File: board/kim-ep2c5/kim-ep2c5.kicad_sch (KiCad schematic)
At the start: 4 parts, among them J101 Conn_02x20_Odd_Even, J102 Conn_01x16_Male, J103 TTY, U101 EP2C5

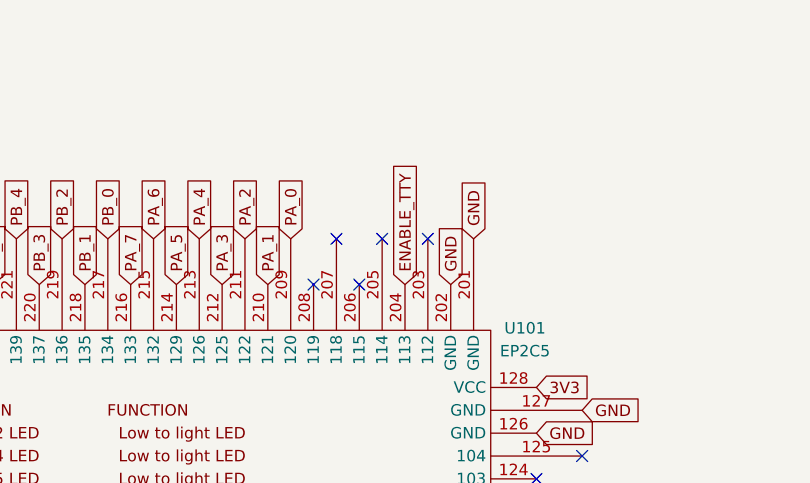
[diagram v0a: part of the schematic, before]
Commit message: Added the serial connection -- oops.
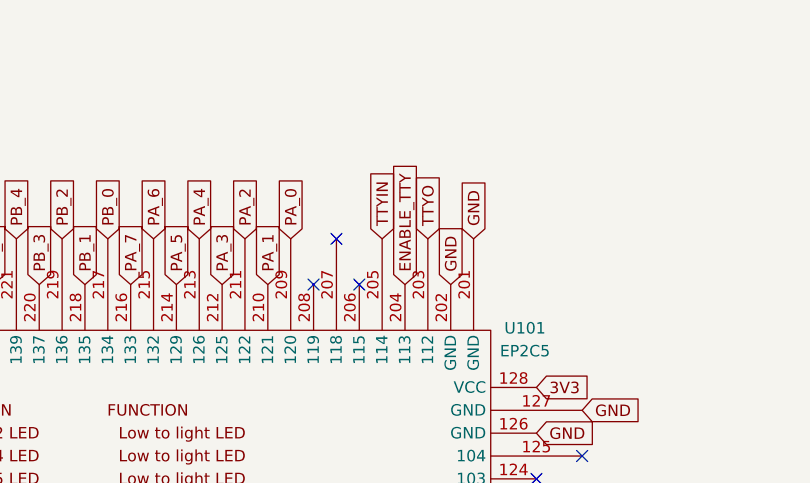
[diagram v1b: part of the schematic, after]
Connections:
- net TTYIN: now also U101.205 (114)
- net TTYO: now also U101.203 (112)
- no-connect marks 45 -> 43
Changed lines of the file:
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@@
   )
   (no_connect (at 115.57 53.975))
-  (no_connect (at 120.65 53.975))
-  (no_connect (at 125.73 53.975))
   (no_connect (at 113.03 59.055))
   (no_connect (at 69.85 53.975))
@@
     )
   )
+  (global_label "TTYIN" (shape input) (at 120.65 53.975 90) (fields_autoplaced)
+    (effects (font (size 1.27 1.27)) (justify left))
+    (property "Intersheet References" "${INTERSHEET_REFS}" (id 0) (at 120.5706 46.6029 90)
+      (effects (font (size 1.27 1.27)) (justify left) hide)
+    )
+  )
   (global_label "TTYIN" (shape input) (at 255.905 85.725 0) (fields_autoplaced)
     (effects (font (size 1.27 1.27)) (justify left))
@@
     )
   )
+  (global_label "TTYO" (shape input) (at 125.73 53.975 90) (fields_autoplaced)
+    (effects (font (size 1.27 1.27)) (justify left))
+    (property "Intersheet References" "${INTERSHEET_REFS}" (id 0) (at 125.6506 47.2076 90)
+      (effects (font (size 1.27 1.27)) (justify left) hide)
+    )
+  )
